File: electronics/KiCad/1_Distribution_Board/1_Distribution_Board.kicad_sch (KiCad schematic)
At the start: 10 parts, among them Q1 DMG2305UX, SW1 SW_Push

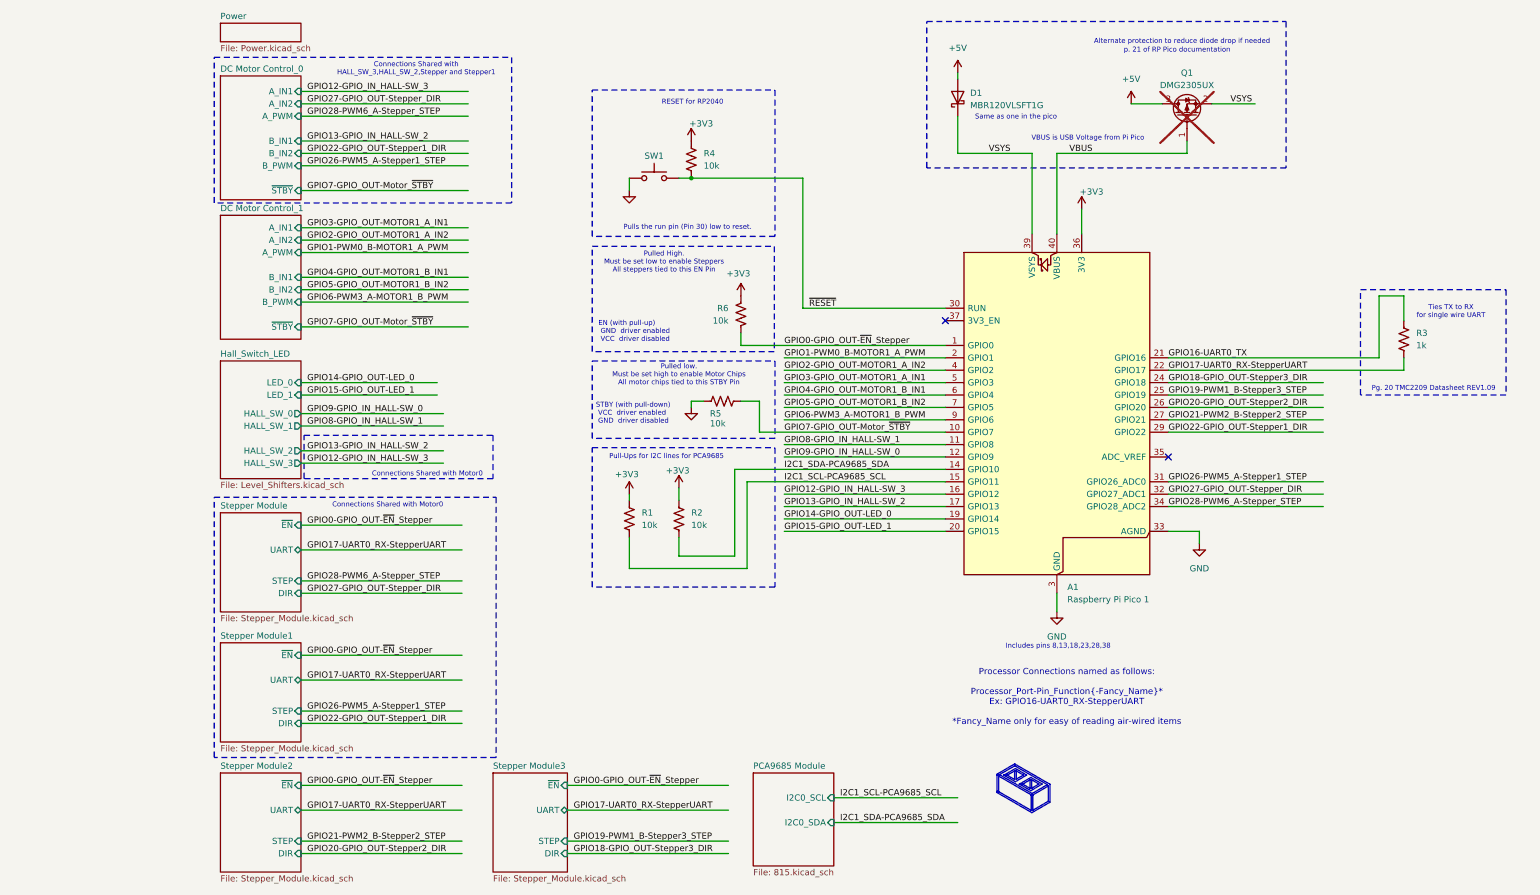
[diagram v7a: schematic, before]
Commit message: Initial start to updates
Removed motor pages, updated Q2,Q3, Cleaned up power module connections.

- Still need to correct routing for these updates.
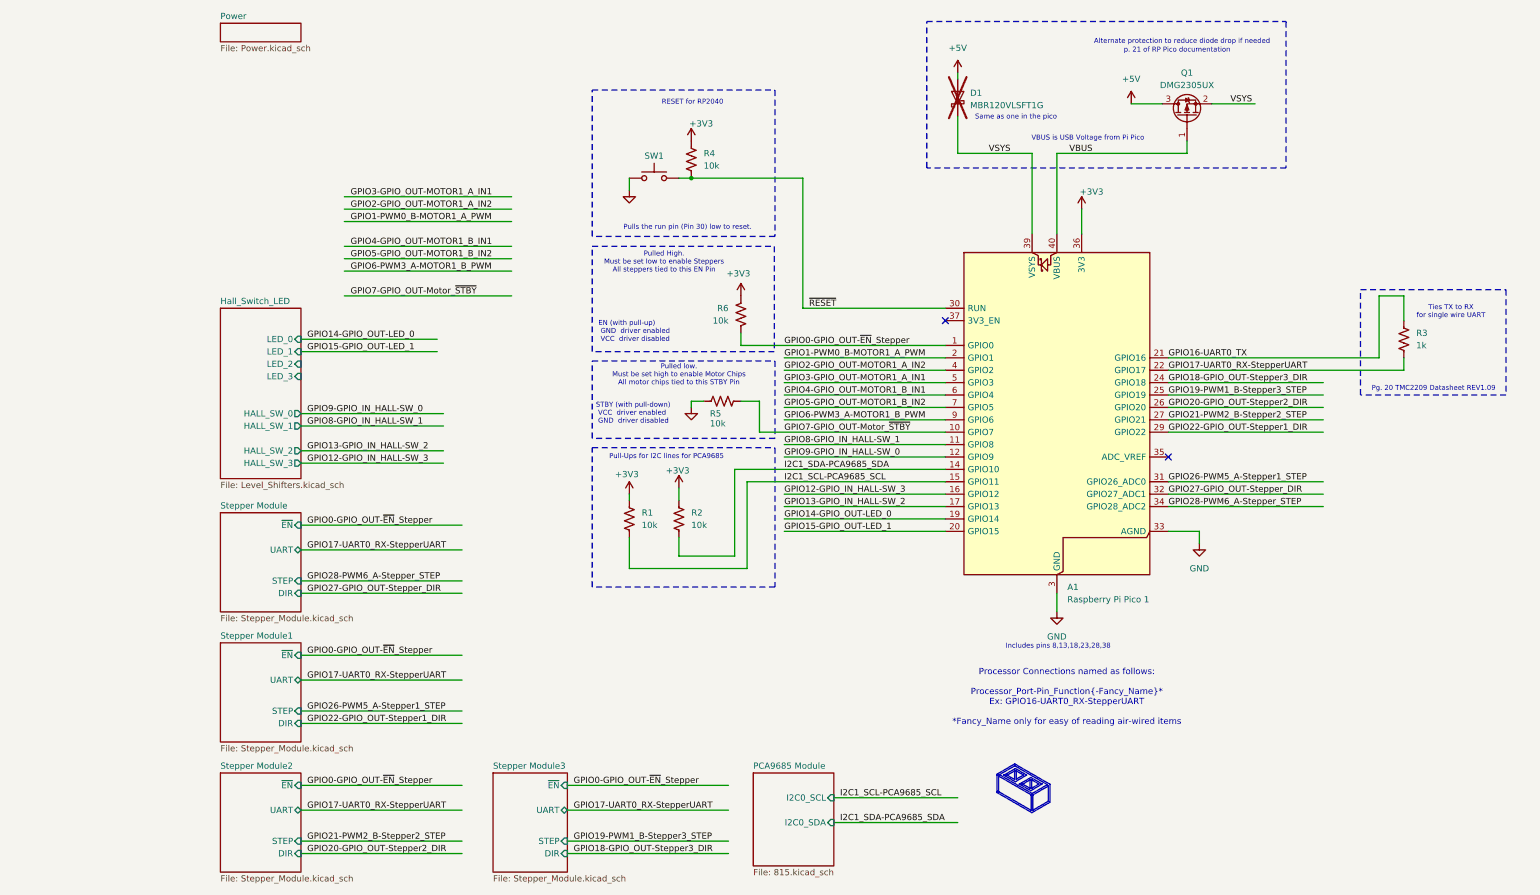
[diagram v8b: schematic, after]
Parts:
- D1: now not fitted
- Q1: now fitted
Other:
- removed sheet DC Motor Control_0
- removed sheet DC Motor Control_1
- sheet Hall_Switch_LED ports: added LED_2, LED_3; removed none
- note removed: "Connections Shared with HALL_SW_3,HALL_SW_2,Stepper and Stepper1"
- note removed: "Connections Shared with Motor0"
